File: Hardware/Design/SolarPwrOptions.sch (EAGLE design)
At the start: 14 parts, among them Q11 DMN3404L, Q12 DMN3404L, U2 OKI-78SR-5/1.5-W36-C

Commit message: Hardware: issue with zener breakdown
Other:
- note added: "3.56A (Isc)"
- note added: "SLP055-12U"
- note added: "WITH BY-PASS DIODES"
- note added: "WITHOUT BY-PASS DIODES"
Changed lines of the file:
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@@
 <text x="94.488" y="-40.64" size="1.778" layer="98">DISCRETE
 PARTS</text>
-<text x="89.408" y="40.64" size="1.778" layer="98">SLP070-12U</text>
-<text x="109.728" y="-7.62" size="1.778" layer="98">SLP070-12U</text>
+<text x="89.154" y="42.164" size="1.778" layer="98">SLP070-12U</text>
+<text x="109.728" y="-6.604" size="1.778" layer="98">SLP055-12U</text>
 <text x="97.028" y="33.02" size="1.778" layer="98">21.6V (Voc)</text>
 <text x="97.028" y="27.94" size="1.778" layer="98">4.35A (Isc)</text>
-<text x="117.348" y="-20.32" size="1.778" layer="98">4.35A (Isc)</text>
+<text x="117.348" y="-20.32" size="1.778" layer="98">3.56A (Isc)</text>
 <text x="117.348" y="-15.24" size="1.778" layer="98">21.6V (Voc)</text>
 <text x="81.788" y="-39.878" size="1.778" layer="98">LA</text>
@@
 <text x="79.248" y="0" size="1.778" layer="98">12V</text>
 <text x="79.248" y="-3.302" size="1.778" layer="98">50AHr</text>
+<text x="89.408" y="38.608" size="1.778" layer="98">WITH BY-PASS DIODES</text>
+<text x="109.728" y="-9.652" size="1.778" layer="98">WITHOUT BY-PASS DIODES</text>
 </plain>
 <instances>

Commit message: Hardware: add aux power input
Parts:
- removed D2: TBD, D-SBR:DSMB
- removed R1: 20K, R-C:R0805
- removed _Q1: TBD, Q-PCH:N-CHDPAK
- removed _Q11: DMN3404L, Q-NCH:N-CHDPAK
- added D3: (no value), D-TVS:TVSSMC
- added Q2: DMP4065S, Q-PCH:N-CHDPAK
- added Q3: BSS138, Q-NCH:N-CHDPAK
- added _D1: TBD, D-SBR:DSMB
- D1: value TBD -> SBR2A40SA
- R2: value 10K -> 50K
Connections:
- removed net IO4: Q11.G, _Q11.G
- removed net N$6: D2.K, R1.2, _Q1.S
- new net IO8: Q11.G, Q3.G
- new net N$1: D1.K, D3.C, Q2.S
- net 0V: now also Q3.S; no longer _Q11.S
- net N$2: now also Q2.D; no longer _Q1.D
- net N$3: now also D3.A, Q2.G, R2.1; no longer R2.2, _Q11.D
- net N$4: now also _D1.K; no longer D1.K
- net N$5: now also Q3.D, R2.2; no longer D2.A, PV2.+PV
- net N$7: now also D1.A, PV2.+PV; no longer R1.1, R2.1, _Q1.G
- net N$8: now also _D1.A; no longer D1.A
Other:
- note added: "1.74A (Isc)"
- note added: "17AHr"
- note added: "ALT"
- note added: "DISCRETE PART"
- note added: "PWR"
- note added: "SLP030-12U"
- note removed: "3.56A (Isc)"
- note removed: "DISCRETE PARTS"
- note removed: "SLP055-12U"
- moved on the sheet: _U2

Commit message: Hardware: solar option
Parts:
- renumbered Q11 to Q15, Q12 to Q14
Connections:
- new net IO4: Q14.G
- net IO7: now also Q15.G; no longer Q14.G
- net IO8: no longer Q15.G
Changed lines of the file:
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@@
 <part name="U2" library="P-DCDC" deviceset="OKI-78SR" device="-H" value="OKI-78SR-5/1.5-W36-C"/>
 <part name="GND1" library="Plane" deviceset="0V" device=""/>
-<part name="Q11" library="Q-NCH" deviceset="N-CH?*" device="DPAK" value="DMN3404L"/>
+<part name="Q15" library="Q-NCH" deviceset="N-CH?*" device="DPAK" value="DMN3404L"/>
 <part name="PV2" library="Documentation" deviceset="PV" device=""/>
 <part name="D1" library="D-SBR" deviceset="D" device="SMB" value="SBR2A40SA"/>
@@
 <part name="Q2" library="Q-PCH" deviceset="N-CH?*" device="DPAK" value="DMP4065S"/>
 <part name="R2" library="R-C" deviceset="R" device="0805" value="50K"/>
-<part name="Q12" library="Q-NCH" deviceset="N-CH?*" device="DPAK" value="DMN3404L"/>
+<part name="Q14" library="Q-NCH" deviceset="N-CH?*" device="DPAK" value="DMN3404L"/>
 <part name="GND3" library="Plane" deviceset="0V" device=""/>
 <part name="D3" library="D-TVS" deviceset="TVS" device="SMC"/>
@@
 <instance part="U2" gate="G$1" x="48.26" y="27.94" rot="MR0"/>
 <instance part="GND1" gate="1" x="33.02" y="0"/>
-<instance part="Q11" gate="G$1" x="48.26" y="7.62"/>
+<instance part="Q15" gate="G$1" x="48.26" y="7.62"/>
 <instance part="PV2" gate="G$1" x="93.98" y="-30.48"/>
 <instance part="D1" gate="G$1" x="71.12" y="-30.48" smashed="yes" rot="R270">
@@
 <attribute name="VALUE" x="54.61" y="-32.258" size="1.27" layer="96" rot="R180"/>
 </instance>
-<instance part="Q12" gate="G$1" x="33.02" y="7.62"/>
+<instance part="Q14" gate="G$1" x="33.02" y="7.62"/>
 <instance part="GND3" gate="1" x="48.26" y="17.78"/>
 <instance part="D3" gate="G$1" x="66.04" y="-33.02" smashed="yes">
@@
 <pinref part="GND1" gate="1" pin="0V"/>
 <junction x="33.02" y="2.54"/>
-<pinref part="Q11" gate="G$1" pin="S"/>
+<pinref part="Q15" gate="G$1" pin="S"/>
 <junction x="48.26" y="2.54"/>
-<pinref part="Q12" gate="G$1" pin="S"/>
+<pinref part="Q14" gate="G$1" pin="S"/>
 </segment>
 <segment>
@@
 <net name="IO8" class="0">
 <segment>
-<pinref part="Q11" gate="G$1" pin="G"/>
-<wire x1="43.18" y1="7.62" x2="43.18" y2="17.78" width="0.1524" layer="91"/>
-<wire x1="43.18" y1="17.78" x2="25.4" y2="17.78" width="0.1524" layer="91"/>
-<label x="25.4" y="17.78" size="1.27" layer="91" rot="R180" xref="yes"/>
-</segment>
-<segment>
 <pinref part="Q3" gate="G$1" pin="G"/>
 <wire x1="30.48" y1="-35.56" x2="27.94" y2="-35.56" width="0.1524" layer="91"/>
@@
 <net name="N$8" class="0">
 <segment>
-<pinref part="Q12" gate="G$1" pin="D"/>
+<pinref part="Q14" gate="G$1" pin="D"/>
 <wire x1="33.02" y1="12.7" x2="33.02" y2="15.24" width="0.1524" layer="91"/>
 <wire x1="33.02" y1="15.24" x2="81.28" y2="15.24" width="0.1524" layer="91"/>
@@
 <junction x="83.82" y="27.94"/>
 <wire x1="83.82" y1="12.7" x2="83.82" y2="27.94" width="0.1524" layer="91"/>
-<pinref part="Q11" gate="G$1" pin="D"/>
+<pinref part="Q15" gate="G$1" pin="D"/>
 <wire x1="48.26" y1="12.7" x2="83.82" y2="12.7" width="0.1524" layer="91"/>
 <wire x1="81.28" y1="15.24" x2="81.28" y2="25.4" width="0.1524" layer="91"/>
@@
 <net name="IO7" class="0">
 <segment>
-<pinref part="Q12" gate="G$1" pin="G"/>
-<wire x1="27.94" y1="7.62" x2="27.94" y2="12.7" width="0.1524" layer="91"/>
-<wire x1="27.94" y1="12.7" x2="25.4" y2="12.7" width="0.1524" layer="91"/>
-<label x="25.4" y="12.7" size="1.27" layer="91" rot="R180" xref="yes"/>
+<pinref part="Q15" gate="G$1" pin="G"/>
+<wire x1="43.18" y1="7.62" x2="43.18" y2="17.78" width="0.1524" layer="91"/>
+<wire x1="43.18" y1="17.78" x2="25.4" y2="17.78" width="0.1524" layer="91"/>
+<label x="25.4" y="17.78" size="1.27" layer="91" rot="R180" xref="yes"/>
 </segment>
 </net>
@@
 </segment>
 </net>
+<net name="IO4" class="0">
+<segment>
+<pinref part="Q14" gate="G$1" pin="G"/>
+<wire x1="27.94" y1="7.62" x2="27.94" y2="12.7" width="0.1524" layer="91"/>
+<wire x1="27.94" y1="12.7" x2="25.4" y2="12.7" width="0.1524" layer="91"/>
+<label x="25.4" y="12.7" size="1.27" layer="91" rot="R180" xref="yes"/>
+</segment>
+</net>

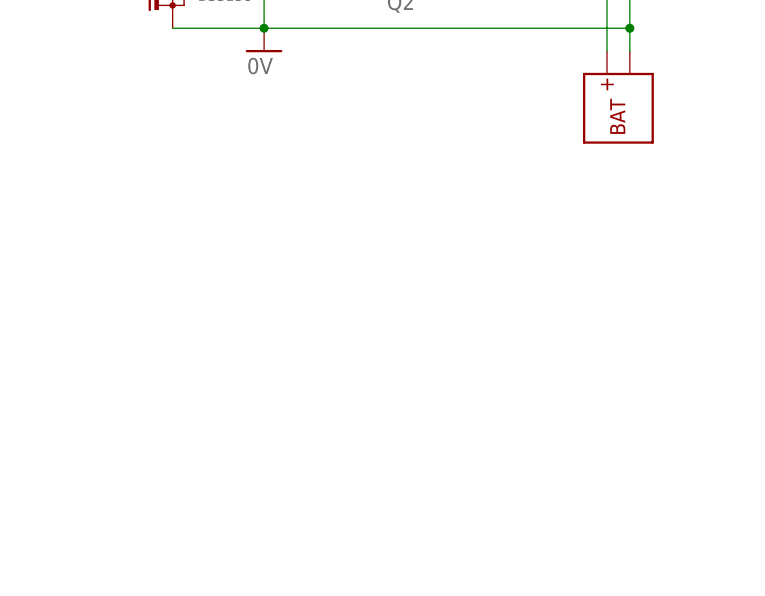
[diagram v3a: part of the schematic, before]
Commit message: Hardware: solar pwr option with ssr
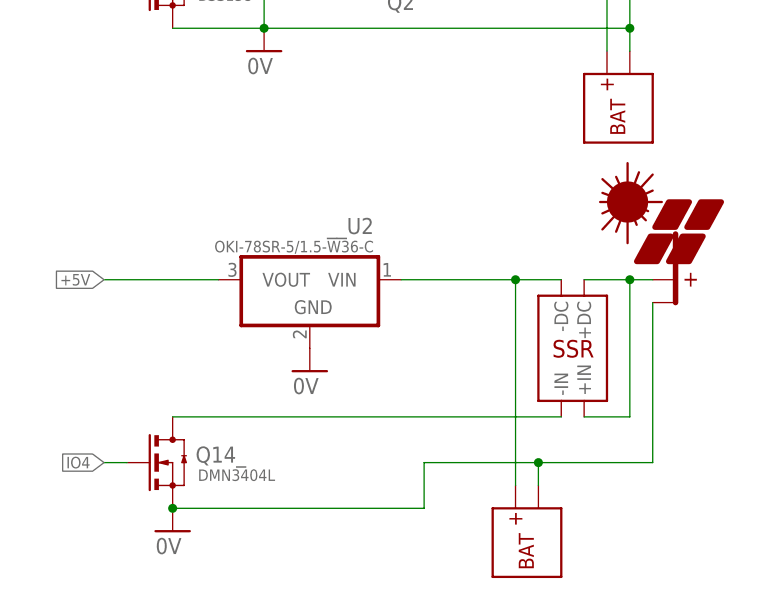
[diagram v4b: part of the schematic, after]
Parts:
- added PV3: PV, Documentation:PV
- added Q14_: DMN3404L, Q-NCH:N-CHDPAK
- added U$2: BAT, Documentation:BAT
- added U$3: SSR_DC, Documentation:SSR_DC
- added __U2: OKI-78SR-5/1.5-W36-C, P-DCDC:OKI-78SR-H
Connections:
- new net N$10: PV3.+PV, U$3.+DC, U$3.+IN
- new net N$6: U$2.+BAT, U$3.-DC, __U2.VIN
- new net N$9: Q14_.D, U$3.-IN
- net +5V: now also __U2.VOUT
- net 0V: now also PV3.-PV, Q14_.S, U$2.-BAT, __U2.GND
- net IO4: now also Q14_.G
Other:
- note added: "2.92A (Isc)"
- note added: "DR06D06"
- note added: "OPEN CIRCUIT WITH SSR"
- note added: "SLP045-12U"
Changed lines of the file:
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@@
 <part name="GND3" library="Plane" deviceset="0V" device=""/>
 <part name="D3" library="D-TVS" deviceset="TVS" device="SMC"/>
+<part name="PV3" library="Documentation" deviceset="PV" device=""/>
+<part name="U$2" library="Documentation" deviceset="BAT" device=""/>
+<part name="__U2" library="P-DCDC" deviceset="OKI-78SR" device="-H" value="OKI-78SR-5/1.5-W36-C"/>
+<part name="GND4" library="Plane" deviceset="0V" device=""/>
+<part name="Q14_" library="Q-NCH" deviceset="N-CH?*" device="DPAK" value="DMN3404L"/>
+<part name="GND5" library="Plane" deviceset="0V" device=""/>
+<part name="U$3" library="Documentation" deviceset="SSR_DC" device=""/>
 </parts>
 <sheets>
@@
 <text x="72.644" y="-21.844" size="1.778" layer="98">PWR</text>
 <text x="73.914" y="-33.782" size="1.778" layer="98">ALT</text>
+<text x="30.48" y="-58.42" size="2.54" layer="98">OPEN CIRCUIT WITH SSR</text>
+<wire x1="20.32" y1="-60.96" x2="66.04" y2="-60.96" width="0.1524" layer="98"/>
+<wire x1="66.04" y1="-60.96" x2="66.04" y2="-101.6" width="0.1524" layer="98"/>
+<wire x1="66.04" y1="-101.6" x2="20.32" y2="-101.6" width="0.1524" layer="98"/>
+<wire x1="20.32" y1="-101.6" x2="20.32" y2="-60.96" width="0.1524" layer="98"/>
+<text x="23.368" y="-63.5" size="1.778" layer="98">ON CIRCUIT BOARD</text>
+<text x="91.694" y="-54.356" size="1.778" layer="98">SLP045-12U</text>
+<text x="99.568" y="-63.5" size="1.778" layer="98">21.6V (Voc)</text>
+<text x="99.568" y="-68.58" size="1.778" layer="98">2.92A (Isc)</text>
+<text x="22.606" y="-84.074" size="1.778" layer="98">AVR PINS</text>
+<text x="81.788" y="-93.218" size="1.778" layer="98">LA</text>
+<text x="81.788" y="-96.52" size="1.778" layer="98">12V</text>
+<text x="81.788" y="-99.822" size="1.778" layer="98">50AHr</text>
+<text x="91.948" y="-57.912" size="1.778" layer="98">WITHOUT BY-PASS DIODES</text>
+<text x="73.914" y="-67.564" size="1.778" layer="98">DR06D06</text>
 </plain>
 <instances>
@@
 <attribute name="VALUE" x="67.31" y="-34.417" size="1.27" layer="96"/>
 </instance>
+<instance part="PV3" gate="G$1" x="91.44" y="-68.58"/>
+<instance part="U$2" gate="G$1" x="76.2" y="-99.06" rot="R90"/>
+<instance part="__U2" gate="G$1" x="50.8" y="-68.58" rot="MR0"/>
+<instance part="GND4" gate="1" x="35.56" y="-96.52"/>
+<instance part="Q14_" gate="G$1" x="35.56" y="-88.9"/>
+<instance part="GND5" gate="1" x="50.8" y="-78.74"/>
+<instance part="U$3" gate="G$1" x="81.28" y="-76.2"/>
 </instances>
 <busses>
@@
 <junction x="86.36" y="-40.64"/>
 </segment>
+<segment>
+<pinref part="GND5" gate="1" pin="0V"/>
+<pinref part="__U2" gate="G$1" pin="GND"/>
+</segment>
+<segment>
+<pinref part="PV3" gate="G$1" pin="-PV"/>
+<wire x1="88.9" y1="-71.12" x2="88.9" y2="-88.9" width="0.1524" layer="91"/>
+<wire x1="88.9" y1="-88.9" x2="76.2" y2="-88.9" width="0.1524" layer="91"/>
+<pinref part="U$2" gate="G$1" pin="-BAT"/>
+<wire x1="76.2" y1="-88.9" x2="63.5" y2="-88.9" width="0.1524" layer="91"/>
+<wire x1="76.2" y1="-91.44" x2="76.2" y2="-88.9" width="0.1524" layer="91"/>
+<junction x="76.2" y="-88.9"/>
+<wire x1="63.5" y1="-88.9" x2="63.5" y2="-93.98" width="0.1524" layer="91"/>
+<wire x1="63.5" y1="-93.98" x2="35.56" y2="-93.98" width="0.1524" layer="91"/>
+<pinref part="GND4" gate="1" pin="0V"/>
+<junction x="35.56" y="-93.98"/>
+<pinref part="Q14_" gate="G$1" pin="S"/>
+</segment>
 </net>
 <net name="+5V" class="0">
@@
 <wire x1="35.56" y1="-22.86" x2="27.94" y2="-22.86" width="0.1524" layer="91"/>
 <label x="27.94" y="-22.86" size="1.27" layer="91" rot="R180" xref="yes"/>
+</segment>
+<segment>
+<pinref part="__U2" gate="G$1" pin="VOUT"/>
+<wire x1="40.64" y1="-68.58" x2="27.94" y2="-68.58" width="0.1524" layer="91"/>
+<label x="27.94" y="-68.58" size="1.27" layer="91" rot="R180" xref="yes"/>
 </segment>
 </net>
@@
 <label x="25.4" y="12.7" size="1.27" layer="91" rot="R180" xref="yes"/>
 </segment>
-</net>
+<segment>
+<pinref part="Q14_" gate="G$1" pin="G"/>
+<wire x1="30.48" y1="-88.9" x2="27.94" y2="-88.9" width="0.1524" layer="91"/>
+<label x="27.94" y="-88.9" size="1.27" layer="91" rot="R180" xref="yes"/>
+</segment>
+</net>
+<net name="N$6" class="0">
+<segment>
+<wire x1="78.74" y1="-68.58" x2="73.66" y2="-68.58" width="0.1524" layer="91"/>
+<pinref part="U$2" gate="G$1" pin="+BAT"/>
+<wire x1="73.66" y1="-91.44" x2="73.66" y2="-68.58" width="0.1524" layer="91"/>
+<junction x="73.66" y="-68.58"/>
+<pinref part="__U2" gate="G$1" pin="VIN"/>
+<wire x1="73.66" y1="-68.58" x2="60.96" y2="-68.58" width="0.1524" layer="91"/>
+<pinref part="U$3" gate="G$1" pin="-DC"/>
+</segment>
+</net>
+<net name="N$9" class="0">
+<segment>
+<pinref part="Q14_" gate="G$1" pin="D"/>
+<wire x1="35.56" y1="-83.82" x2="78.74" y2="-83.82" width="0.1524" layer="91"/>
+<pinref part="U$3" gate="G$1" pin="-IN"/>
+</segment>
+</net>
+<net name="N$10" class="0">
+<segment>
+<pinref part="PV3" gate="G$1" pin="+PV"/>
+<wire x1="88.9" y1="-68.58" x2="86.36" y2="-68.58" width="0.1524" layer="91"/>
+<wire x1="86.36" y1="-68.58" x2="81.28" y2="-68.58" width="0.1524" layer="91"/>
+<junction x="86.36" y="-68.58"/>
+<pinref part="U$3" gate="G$1" pin="+DC"/>
+<pinref part="U$3" gate="G$1" pin="+IN"/>
+<wire x1="81.28" y1="-83.82" x2="86.36" y2="-83.82" width="0.1524" layer="91"/>
+<wire x1="86.36" y1="-83.82" x2="86.36" y2="-68.58" width="0.1524" layer="91"/>
+</segment>
+</net>
